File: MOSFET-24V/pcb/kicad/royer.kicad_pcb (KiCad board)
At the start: 2 copper layers, 24 parts, among them J1 9-24V, J2 COIL, Q1 IRFB4410, Q2 IRFD110, Q3 IRFD110, Q4 IRFB4410

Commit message: net labels
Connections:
- net Net-(C1-Pad1) renamed /D1
- net Net-(C1-Pad2) renamed /C1
- net Net-(C3-Pad1) renamed /D2
- net Net-(C4-Pad2) renamed /C2
- net Net-(C5-Pad1) renamed /9V
- net Net-(D2-Pad1) renamed /X1
- net Net-(D3-Pad1) renamed /X2
- net Net-(J1-Pad2) renamed /24V
- net Net-(Q1-Pad1) renamed /G1
- net Net-(Q4-Pad1) renamed /G2

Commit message: rearranging SMD components
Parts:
- C5: footprint Capacitors_ThroughHole:C_Rect_L27_W9_H17_P23 -> Capacitors_SMD:c_elec_4x5.8; moved to B.Cu
- C6: footprint Capacitors_ThroughHole:C_Rect_L27_W9_H17_P23 -> Capacitors_SMD:C_1206_HandSoldering; moved to B.Cu
- D1, D4: footprint Diodes_SMD:MELF_Handsoldering -> Diodes_SMD:MiniMELF_Handsoldering
- Q1, Q4: footprint Housings_DIP:DIP-4_W7.62mm_LongPads -> TO_SOT_Packages_THT:TO-220_Neutral123_Vertical_LargePads
- Q2, Q3: footprint TO_SOT_Packages_THT:TO-220_Neutral123_Vertical_LargePads -> Housings_DIP:DIP-4_W7.62mm_LongPads
- moved R7 52.1 mm to (184.2, 57.1), turned to 0 degrees
- moved J1 47.0 mm to (182.9, 43.2)
- moved D4 39.2 mm to (176.5, 62.2), turned to 270 degrees
- moved C1 38.7 mm to (152.4, 61.0), turned to 90 degrees
- moved C3 35.9 mm to (181.6, 63.5), turned to 180 degrees
- moved D1 35.8 mm to (154.9, 62.2), turned to 270 degrees
- moved C4 35.6 mm to (174.0, 61.0), turned to 90 degrees
- moved C2 35.3 mm to (160.0, 66.0), turned to 0 degrees
- moved Q3 34.2 mm to (172.7, 66.0), turned to 270 degrees
- moved R2 33.0 mm to (144.8, 59.0), turned to 90 degrees
- moved Q2 33.0 mm to (151.1, 66.0), turned to 270 degrees
- moved R4 30.7 mm to (144.8, 66.0), turned to 90 degrees
- moved R5 30.5 mm to (181.6, 66.0), turned to 0 degrees
- moved R3 29.6 mm to (166.4, 64.8), turned to 90 degrees
- moved C5 29.5 mm to (189.2, 64.8), turned to 270 degrees
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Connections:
- J2 pad 1: /C2 -> /C1
- J2 pad 3: /C1 -> /C2
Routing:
- net /C1: track 110.6 -> 28.6 mm, vias 1 -> 0
- net /D1: track 90.1 -> 16.5 mm
- net GND: track 155.6 -> 82.1 mm, vias 2 -> 0
- net /X1: track 91.3 -> 34.2 mm
- net /9V: track 112.2 -> 61.7 mm, vias 0 -> 1
- net /C2: track 81.6 -> 31.9 mm, vias 1 -> 0
- net /X2: track 74.6 -> 33.3 mm
- net /D2: track 69.5 -> 35.5 mm
- net /G1: track 27.3 -> 7.32 mm, vias 2 -> 0
- net /G2: track 20.4 -> 5.30 mm
- net /24V: track 54.9 -> 48.9 mm

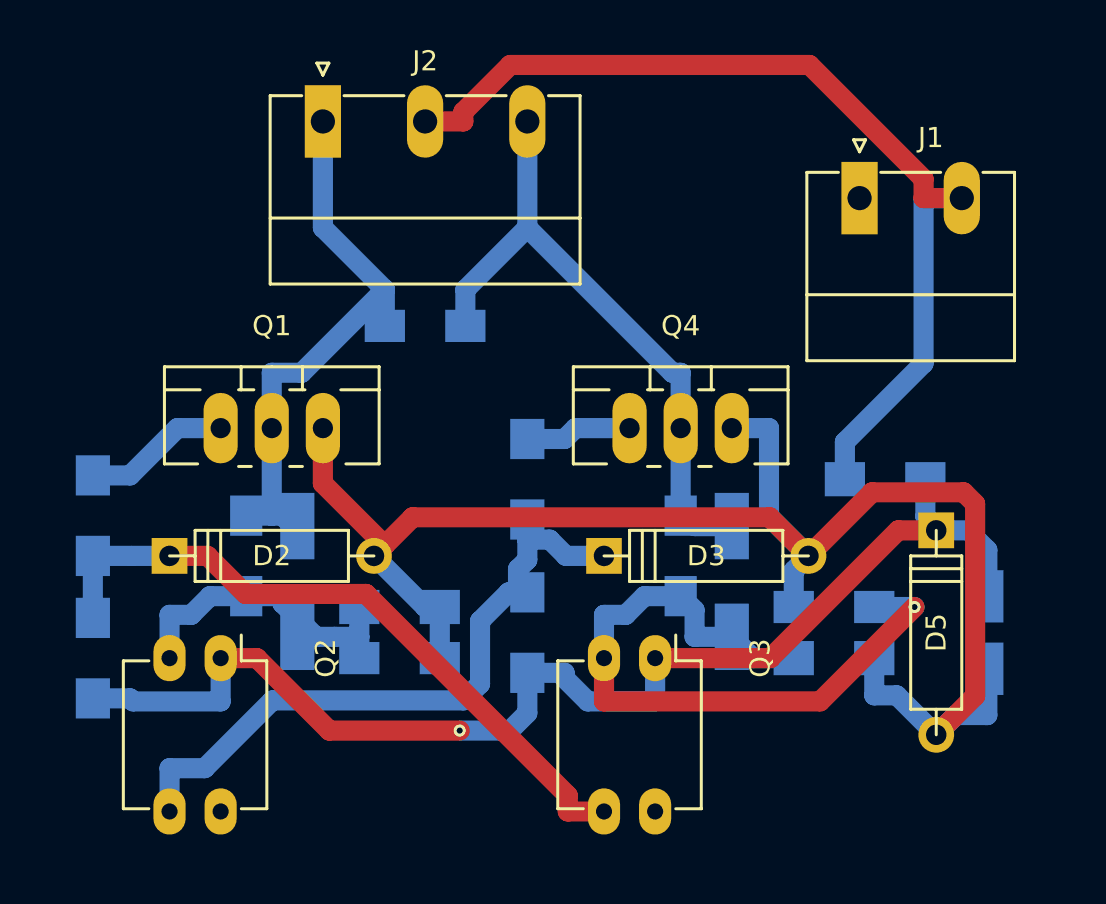
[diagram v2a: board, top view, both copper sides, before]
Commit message: fixing GND on the schematics
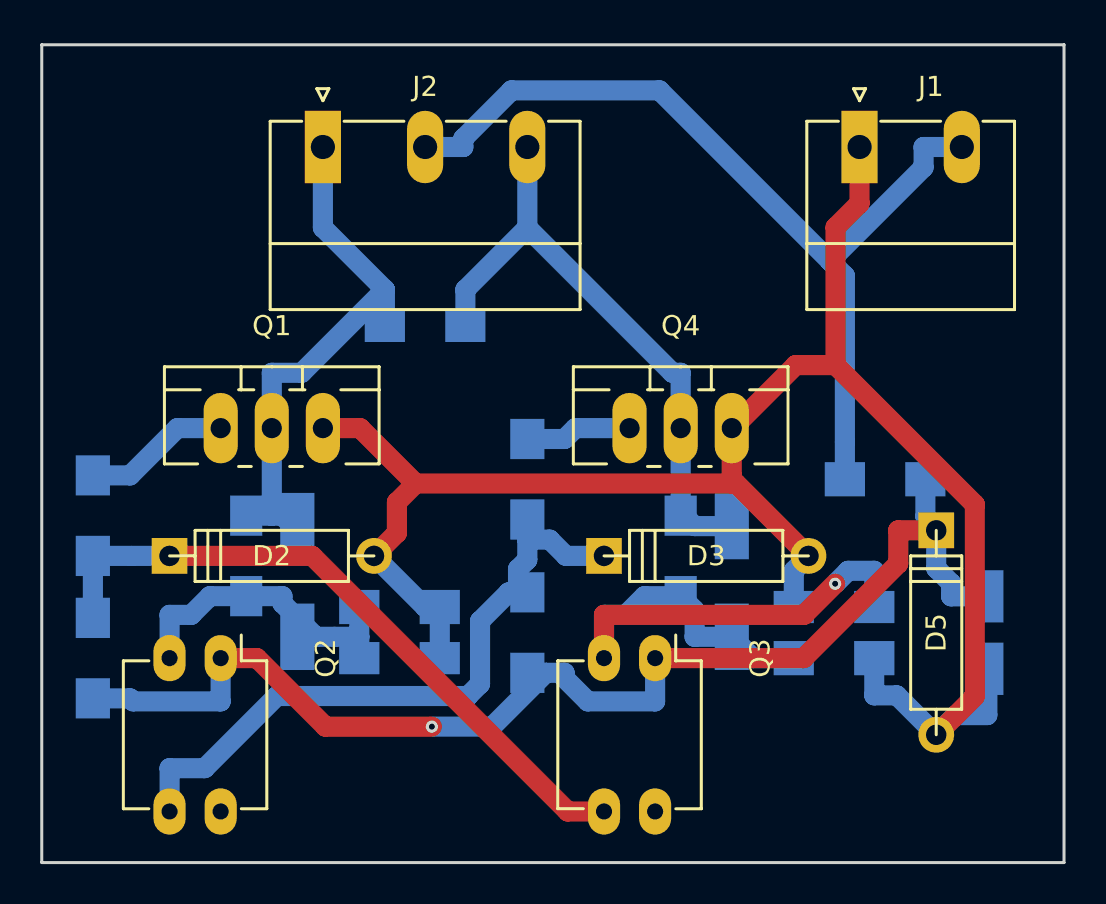
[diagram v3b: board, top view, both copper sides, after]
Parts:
- moved J1 2.54 mm to (182.9, 40.6)
- moved J2 1.27 mm to (156.2, 40.6)
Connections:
- J1 pad 1: (no net) -> GND
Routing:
- net GND: track 82.1 -> 94.5 mm
- net /D2: track 35.5 -> 32.3 mm
- net /24V: track 48.9 -> 45.7 mm
- net /C2: track 31.9 -> 30.6 mm
- net /C1: track 28.6 -> 27.4 mm
- net /9V: track 61.7 -> 62.2 mm
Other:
- board outline added: 50.8 x 40.6 mm

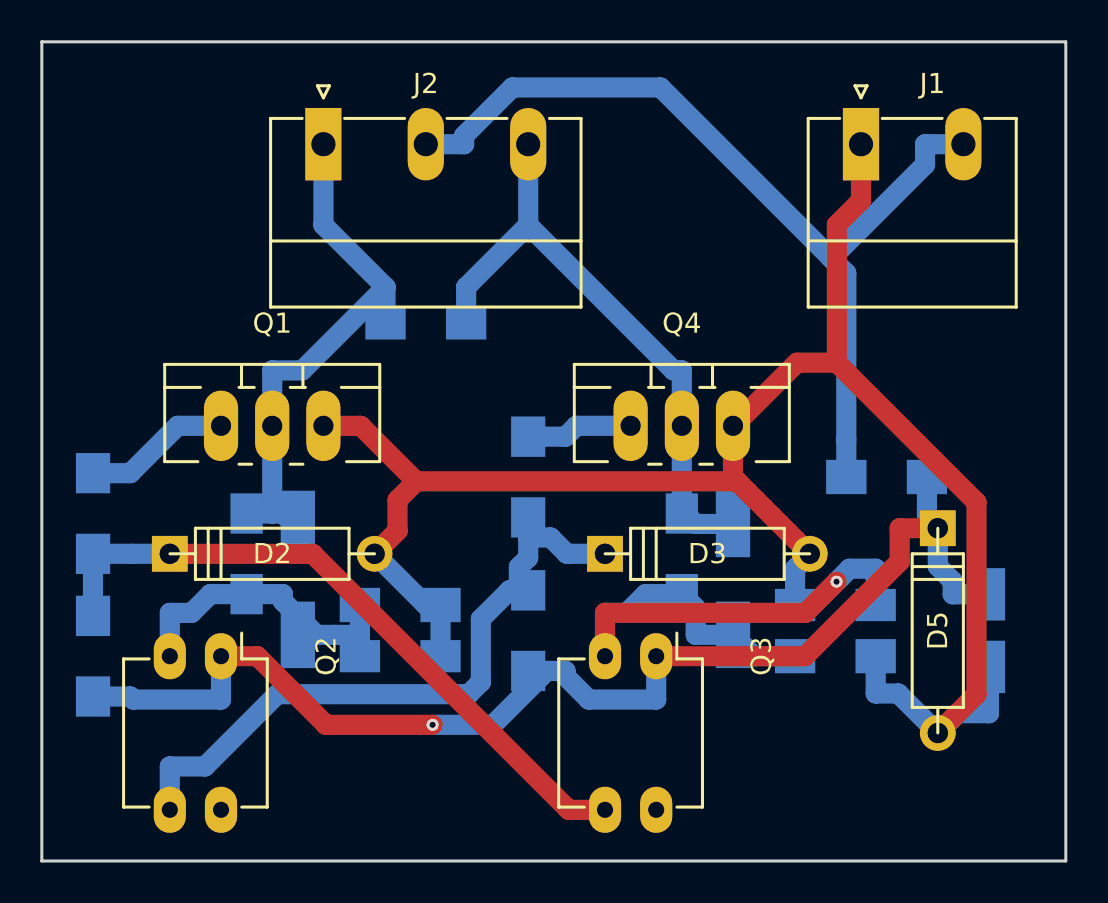
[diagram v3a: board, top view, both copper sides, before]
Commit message: better component placement, single-sided PCB
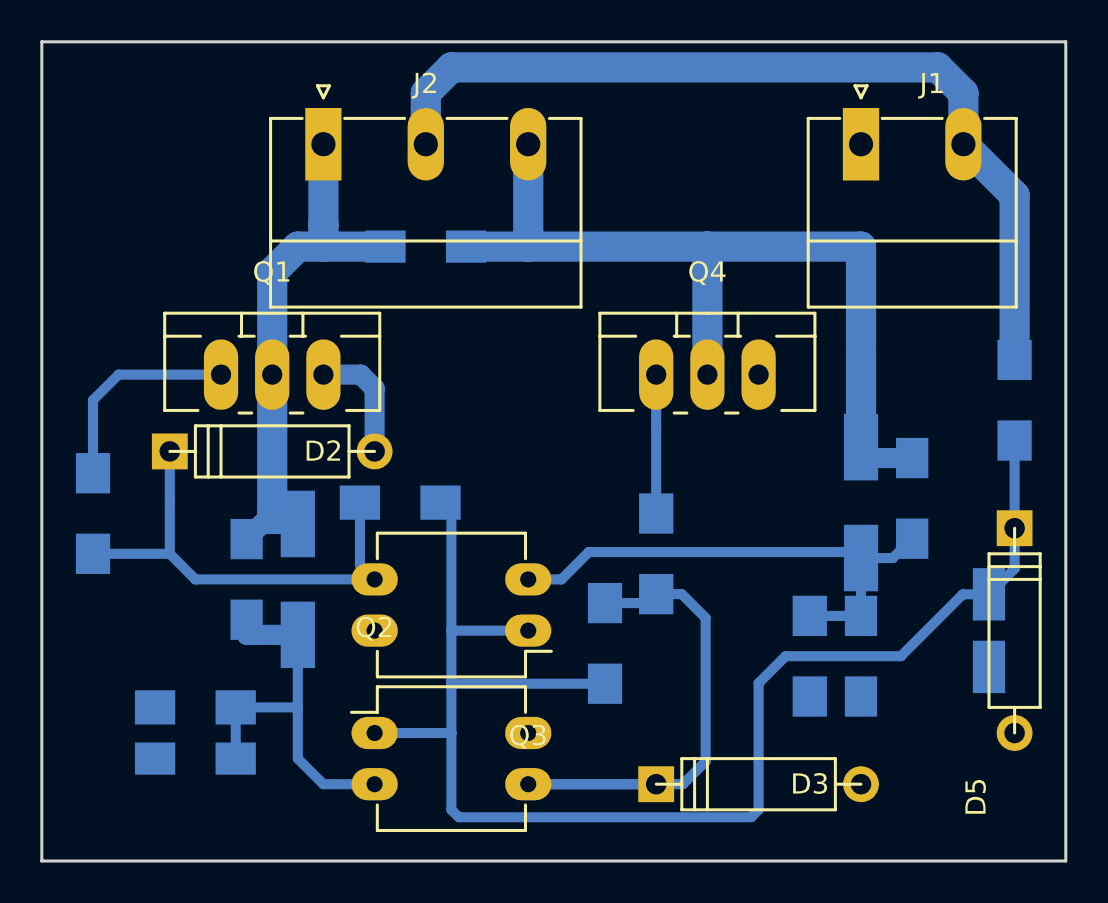
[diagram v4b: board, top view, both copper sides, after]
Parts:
- moved R4 17.0 mm to (160.0, 58.4), turned to 180 degrees
- moved C4 11.8 mm to (185.4, 58.2)
- moved D3 11.7 mm to (177.8, 72.4)
- moved C2 11.4 mm to (149.9, 71.1), turned to 180 degrees
- moved R1 11.4 mm to (149.9, 68.6), turned to 180 degrees
- moved Q2 8.52 mm to (158.8, 69.8), turned to 0 degrees
- moved R6 7.41 mm to (172.7, 61.0)
- moved D4 7.41 mm to (182.9, 58.4)
- moved R7 7.41 mm to (190.5, 53.3), turned to 270 degrees
- moved Q3 6.48 mm to (166.4, 64.8), turned to 180 degrees
- moved D2 5.08 mm to (153.7, 55.9)
- moved R3 3.86 mm to (170.2, 65.4)
- moved C6 3.81 mm to (161.3, 45.7)
- moved D5 3.81 mm to (190.5, 64.8)
- moved C3 2.84 mm to (182.9, 66.0), turned to 270 degrees
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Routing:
- net GND: track 94.5 -> 5.95 mm
- net /C2: track 30.6 -> 43.7 mm
- net /9V: track 62.2 -> 74.2 mm, vias 1 -> 0
- net /X1: track 33.7 -> 23.7 mm
- net /D2: track 32.3 -> 25.5 mm, vias 1 -> 0
- net /X2: track 33.3 -> 28.4 mm
- net /G1: track 7.32 -> 10.5 mm
- net /D1: track 16.5 -> 18.3 mm
- net /G2: track 5.30 -> 6.89 mm
- net /24V: track 45.7 -> 44.6 mm
- added copper zone on B.Cu, net GND
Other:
- net class Default: trace_width 1 -> 0.5
- net class Power added: clearance 0.5, trace_width 1.5, via_dia 0.6, via_drill 0.4
- rule trace_min: 0.2 -> 0.127
- rule via_min_drill: 0.3 -> 0.254
- rule via_min_size: 0.4 -> 0.454

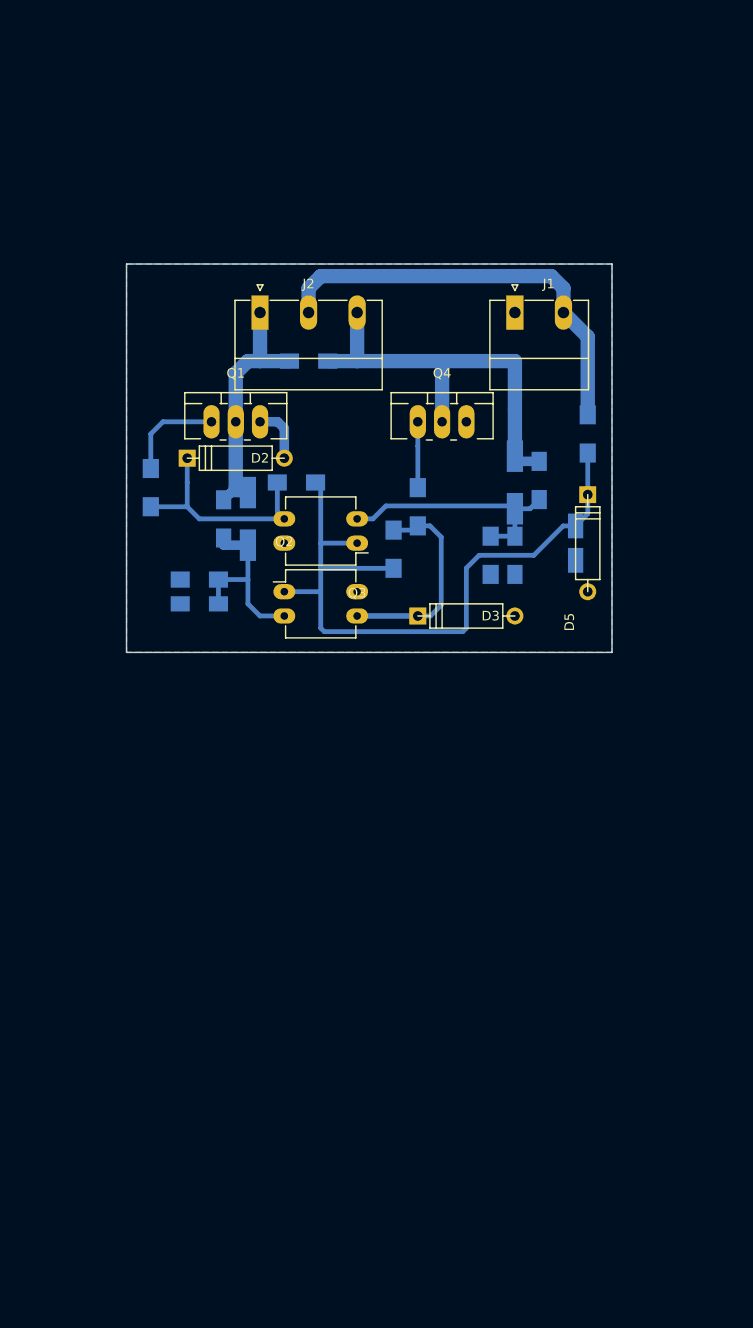
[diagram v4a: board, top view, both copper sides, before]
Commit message: symmetry on the PCB
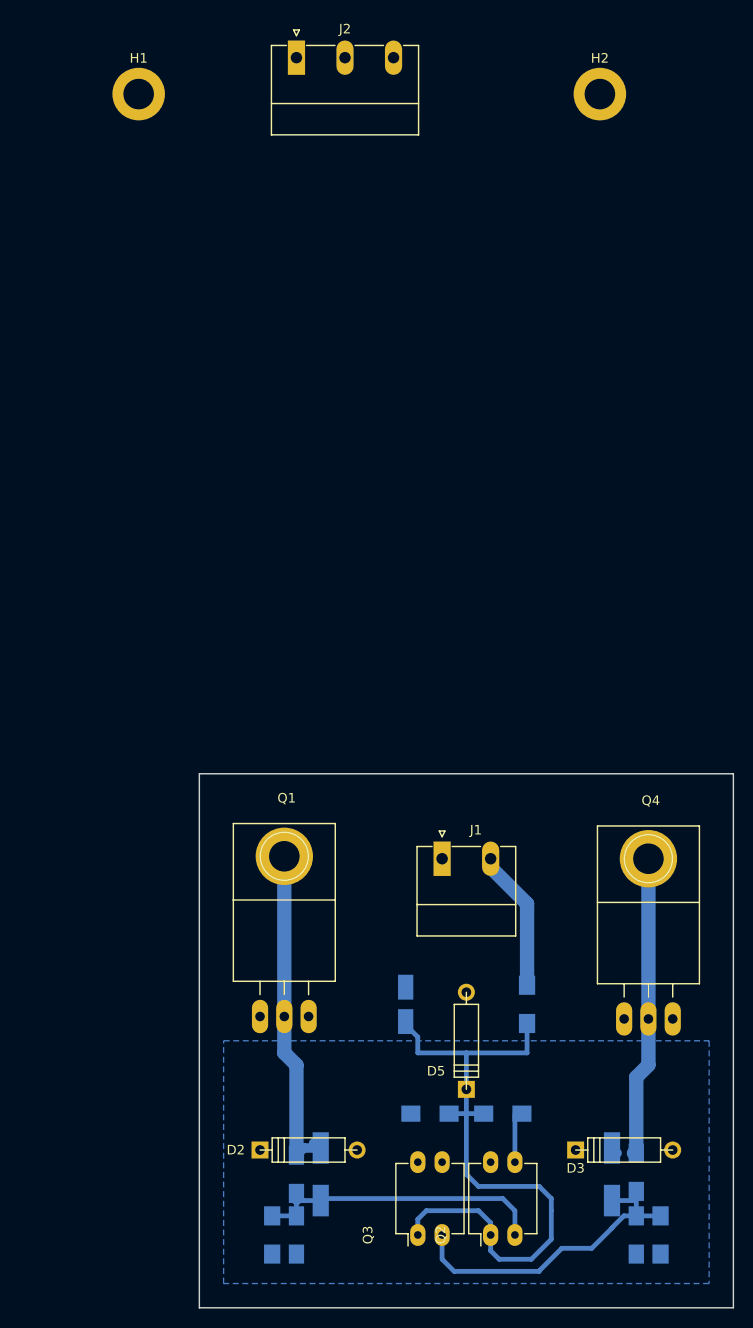
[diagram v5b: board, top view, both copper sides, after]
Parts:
- removed C6: 2uF, Capacitors_SMD:C_1206_HandSoldering
- removed R2, R6: 0, Resistors_SMD:R_1206_HandSoldering
- added H1: 3.2mm, Mounting_Holes:MountingHole_3.2mm_M3_ISO14580_Pad, F.Cu at (143.5, 17.8)
- added H2: 3.2mm, Mounting_Holes:MountingHole_3.2mm_M3_ISO14580_Pad, F.Cu at (191.8, 17.8)
- Q1, Q4: footprint TO_SOT_Packages_THT:TO-220_Neutral123_Vertical_LargePads -> TO-220:TO-220_Neutral123_Horizontal_LargePads
- moved R5 73.3 mm to (198.1, 137.2)
- moved D4 73.1 mm to (193.0, 130.8)
- moved C4 73.1 mm to (195.6, 130.6)
- moved D2 72.8 mm to (161.3, 128.3)
- moved Q3 72.7 mm to (172.7, 137.2), turned to 90 degrees
- moved C3 72.2 mm to (195.6, 137.2)
- moved Q2 70.7 mm to (180.3, 137.2), turned to 90 degrees
- moved C1 69.0 mm to (160.0, 130.8)
- moved D1 69.0 mm to (162.6, 130.8)
- moved R1 69.0 mm to (157.5, 137.2), turned to 270 degrees
- moved R4 67.5 mm to (174.0, 124.5)
- moved C2 66.8 mm to (160.0, 137.2), turned to 270 degrees
- moved Q4 66.1 mm to (196.8, 114.6)
- moved Q1 62.4 mm to (158.8, 114.3)
- moved R3 60.2 mm to (181.6, 124.5), turned to 0 degrees
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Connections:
- D2 pad 1: /X1 -> /G1
- D3 pad 1: /X2 -> /G2
- Q2 pad 3: /X2 -> /G2
- Q3 pad 3: /X1 -> /G1
- R3 pad 2: /X2 -> /G2
- R4 pad 2: /X1 -> /G1
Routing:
- net /24V: track 44.6 -> 14.8 mm
- net /X2: track 28.4 -> 0.00 mm
- net /X1: track 23.7 -> 0.00 mm
- net /D1: track 18.3 -> 32.0 mm
- net /C2: track 43.7 -> 32.3 mm
- net /G1: track 10.5 -> 1.53 mm
- net /C1: track 27.5 -> 35.6 mm
- net /D2: track 25.5 -> 33.6 mm
- net GND: track 5.95 -> 0.00 mm
- net /9V: track 74.2 -> 69.5 mm
- net /G2: track 6.89 -> 5.08 mm
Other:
- board size 50.8 x 40.6 mm -> 55.9 x 55.9 mm

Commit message: rearranging components, routed
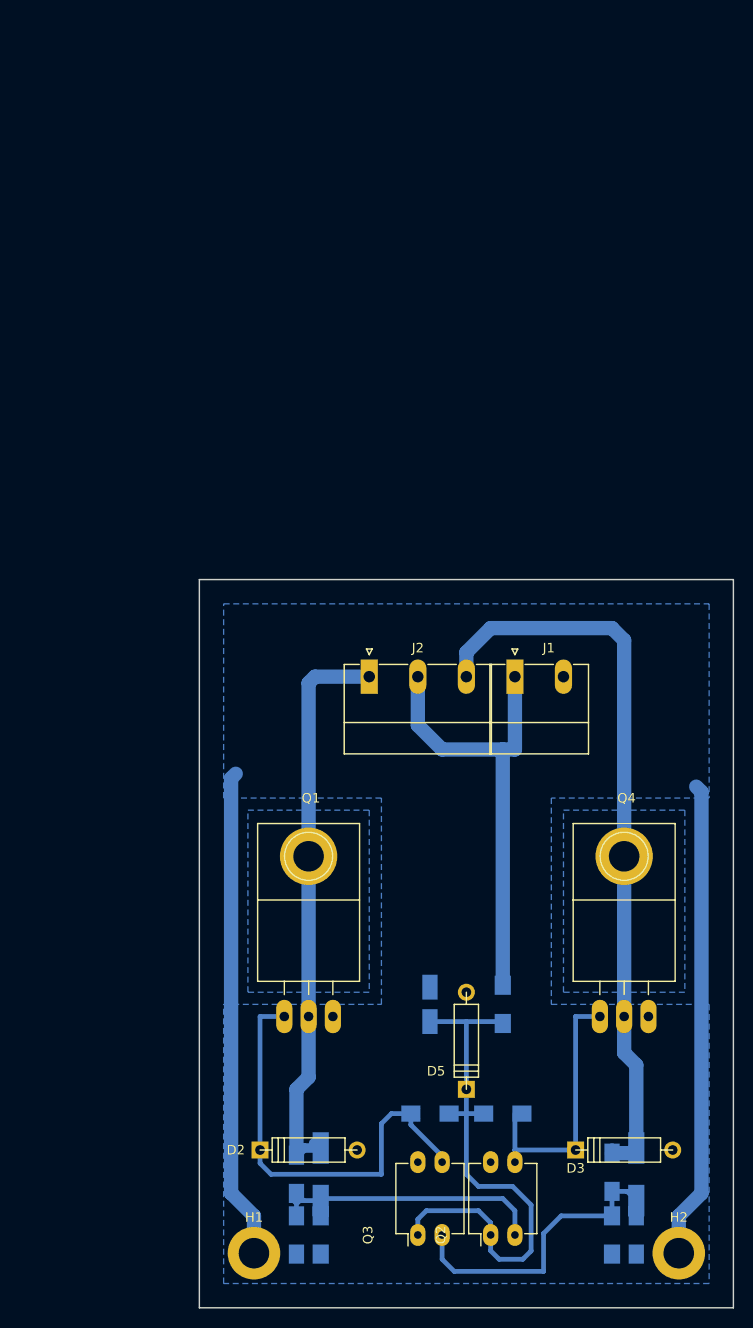
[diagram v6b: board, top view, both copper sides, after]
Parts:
- moved H1 121.9 mm to (155.6, 139.1)
- moved H2 121.6 mm to (200.0, 139.1)
- moved J2 65.2 mm to (167.6, 78.7)
- moved J1 20.5 mm to (182.9, 78.7)
- moved R1 5.08 mm to (162.6, 137.2)
- moved R5 5.08 mm to (193.0, 137.2)
- moved Q4 2.55 mm to (194.3, 114.3)
- moved C4 2.54 mm to (193.0, 130.6)
- moved C5 2.54 mm to (174.0, 113.0)
- moved D4 2.54 mm to (195.6, 130.8)
- moved Q1 2.54 mm to (161.3, 114.3)
- moved R7 2.54 mm to (181.6, 113.0)
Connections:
- J1 pad 1: GND -> /24V
- J1 pad 2: /24V -> GND
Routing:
- net GND: track 0.00 -> 101.4 mm
- net /G1: track 1.53 -> 47.9 mm
- net /C2: track 32.3 -> 78.6 mm
- net /24V: track 14.8 -> 48.6 mm
- net /C1: track 35.6 -> 60.4 mm
- net /G2: track 5.08 -> 27.9 mm
- net /9V: track 69.5 -> 58.3 mm
- net /D1: track 32.0 -> 29.5 mm
- net /D2: track 33.6 -> 34.2 mm
- added copper zone on B.Cu, net /C1
- added copper zone on B.Cu, net /C2
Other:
- board size 55.9 x 55.9 mm -> 55.9 x 76.2 mm

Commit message: optimizing component placement
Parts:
- added H3: 3.2mm, Mounting_Holes:MountingHole_3.2mm_M3_ISO14580_Pad, F.Cu at (200.0, 74.3)
- added H4: 3.2mm, Mounting_Holes:MountingHole_3.2mm_M3_ISO14580_Pad, F.Cu at (155.6, 74.3)
- moved C3 5.08 mm to (190.5, 137.2)
- moved D2 2.54 mm to (163.8, 128.3)
- moved D4 2.54 mm to (193.0, 130.8)
- moved C1 2.54 mm to (162.6, 130.8)
- moved C2 2.54 mm to (162.6, 137.2)
- moved C4 2.54 mm to (190.5, 130.6)
- moved D1 2.54 mm to (165.1, 130.8)
- moved D3 2.54 mm to (191.8, 128.3)
- moved R1 2.54 mm to (165.1, 137.2)
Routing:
- net /G1: track 47.9 -> 42.9 mm
- net /G2: track 27.9 -> 30.6 mm
- net /C1: track 60.4 -> 59.6 mm
- net /C2: track 78.6 -> 78.1 mm
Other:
- board size 55.9 x 76.2 mm -> 53.3 x 73.7 mm
